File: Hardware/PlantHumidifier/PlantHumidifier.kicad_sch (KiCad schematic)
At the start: 9 parts

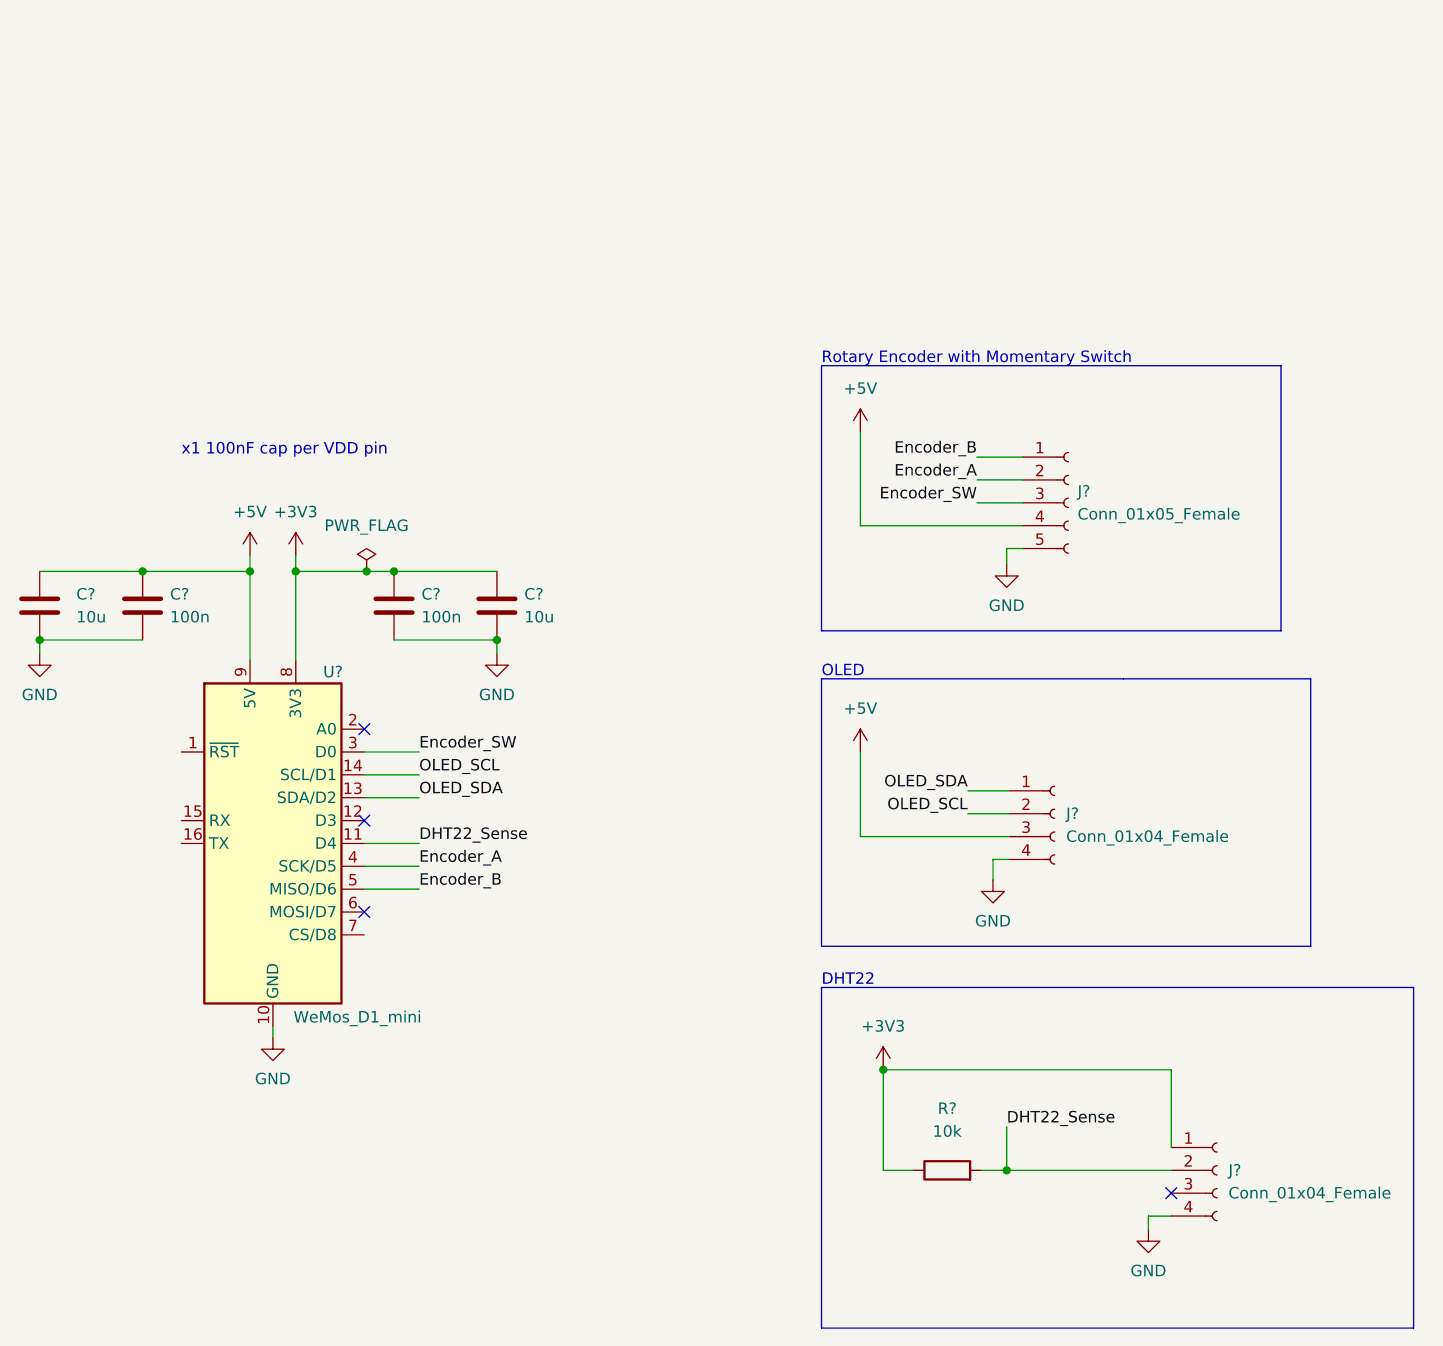
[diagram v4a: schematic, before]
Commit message: Schematic: Finish wiring Grove water atomizer
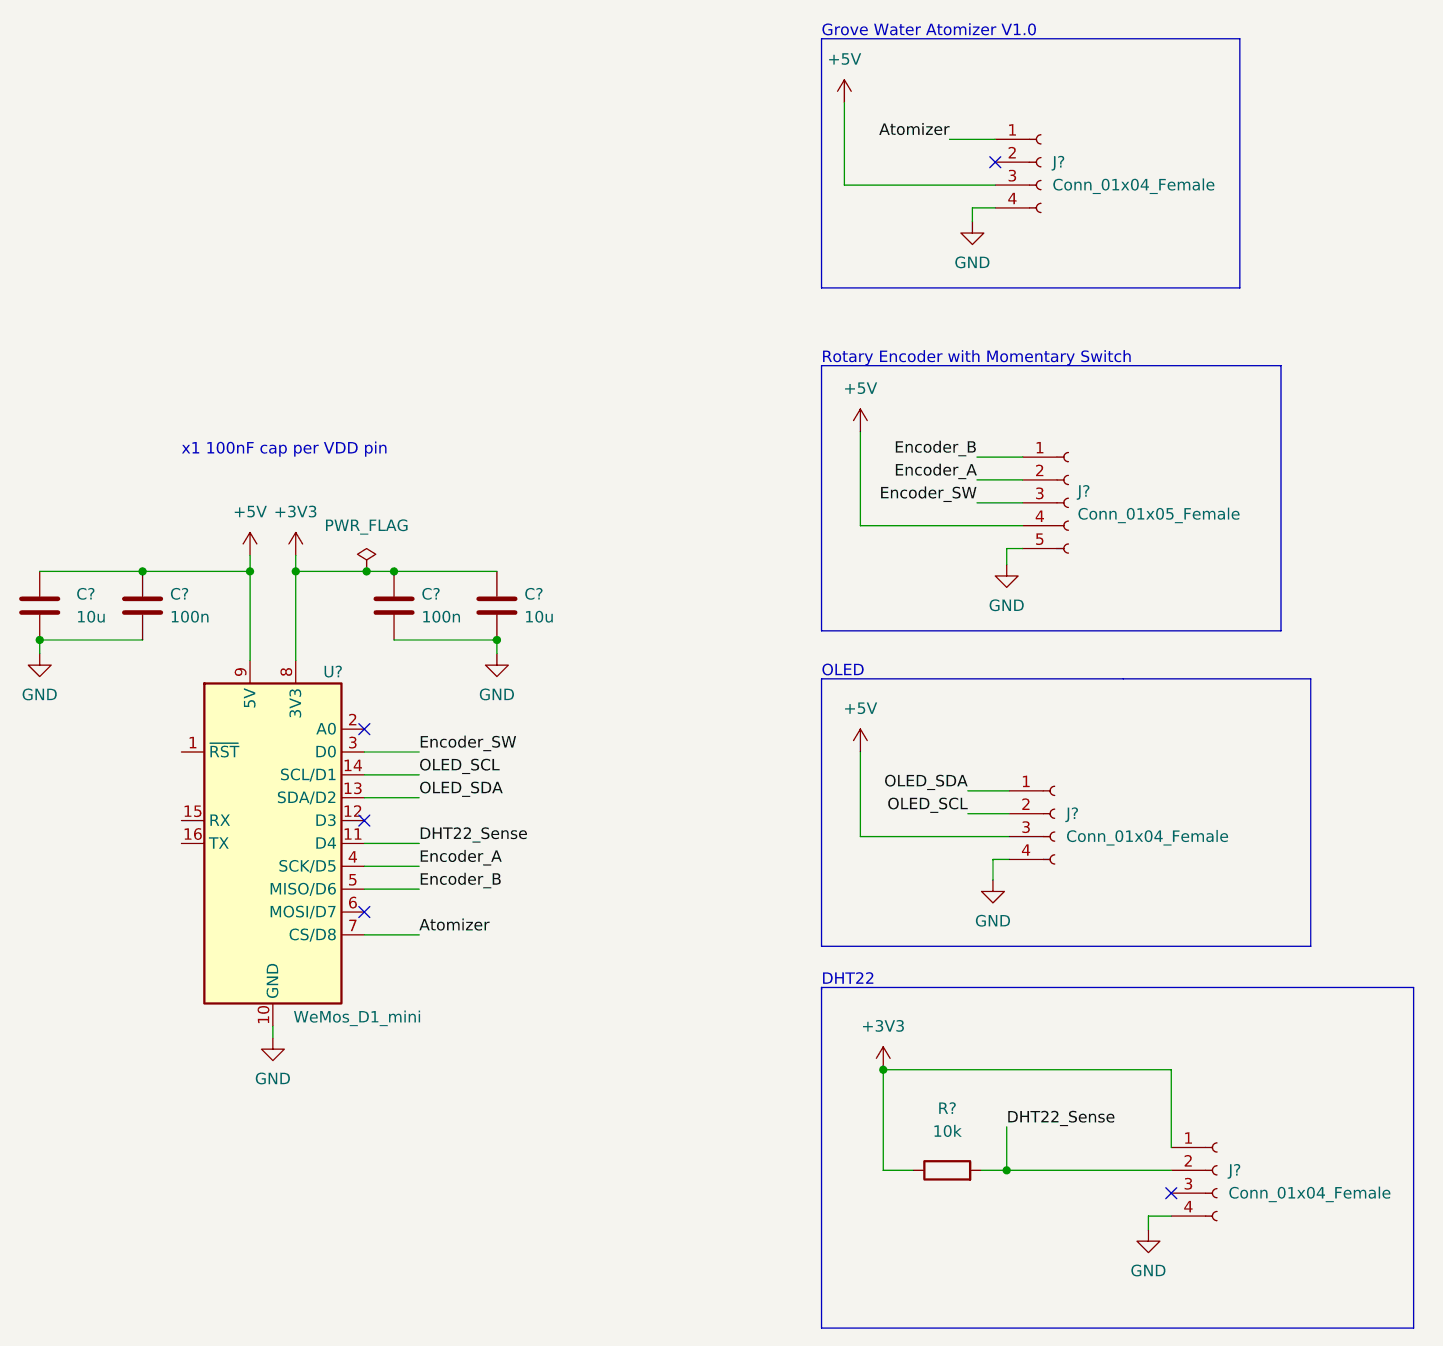
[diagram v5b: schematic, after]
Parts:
- added J?: Conn_01x04_Female, symbol Connector:Conn_01x04_Female
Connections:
- net +5V: now also J?.3 (Pin_3)
- net GND: now also J?.4 (Pin_4)
- net Atomizer: now reaches U?.7 (CS/D8)
- net Atomizer: now also J?.1 (Pin_1)
- no-connect marks 4 -> 5
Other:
- note added: "Grove Water Atomizer V1.0"
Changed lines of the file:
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@@
   (junction (at 164.592 77.724) (diameter 0) (color 0 0 0 0)
   )
+  (no_connect (at 231.394 32.258))
   (no_connect (at 161.29 105.41))
   (no_connect (at 250.952 146.812))
@@
     (stroke (width 0) (type default) (color 0 0 0 0))
   )
+  (wire (pts (xy 228.854 38.862) (xy 228.854 37.338))
+    (stroke (width 0) (type default) (color 0 0 0 0))
+  )
   (polyline (pts (xy 212.09 123.952) (xy 277.876 123.952))
     (stroke (width 0) (type default) (color 0 0 0 0))
@@
     (stroke (width 0) (type default) (color 0 0 0 0))
   )
+  (polyline (pts (xy 258.572 18.542) (xy 212.09 18.542))
+    (stroke (width 0) (type default) (color 0 0 0 0))
+  )
   (wire (pts (xy 228.346 102.108) (xy 232.918 102.108))
     (stroke (width 0) (type default) (color 0 0 0 0))
@@
     (stroke (width 0) (type default) (color 0 0 0 0))
   )
+  (polyline (pts (xy 212.09 18.542) (xy 212.09 46.228))
+    (stroke (width 0) (type default) (color 0 0 0 0))
+  )
   (wire (pts (xy 161.544 77.724) (xy 164.592 77.724))
     (stroke (width 0) (type default) (color 0 0 0 0))
@@
     (stroke (width 0) (type default) (color 0 0 0 0))
   )
+  (wire (pts (xy 226.314 29.718) (xy 231.394 29.718))
+    (stroke (width 0) (type default) (color 0 0 0 0))
+  )
   (wire (pts (xy 161.29 107.95) (xy 167.386 107.95))
     (stroke (width 0) (type default) (color 0 0 0 0))
@@
     (stroke (width 0) (type default) (color 0 0 0 0))
   )
+  (polyline (pts (xy 258.572 46.228) (xy 258.572 18.542))
+    (stroke (width 0) (type default) (color 0 0 0 0))
+  )
   (wire (pts (xy 148.59 77.724) (xy 148.59 87.63))
     (stroke (width 0) (type default) (color 0 0 0 0))
@@
     (stroke (width 0) (type default) (color 0 0 0 0))
   )
+  (wire (pts (xy 161.29 118.11) (xy 167.386 118.11))
+    (stroke (width 0) (type default) (color 0 0 0 0))
+  )
+  (polyline (pts (xy 212.09 46.228) (xy 258.572 46.228))
+    (stroke (width 0) (type default) (color 0 0 0 0))
+  )
   (wire (pts (xy 125.222 77.724) (xy 136.652 77.724))
     (stroke (width 0) (type default) (color 0 0 0 0))
@@
     (stroke (width 0) (type default) (color 0 0 0 0))
   )
+  (wire (pts (xy 214.63 25.654) (xy 214.63 34.798))
+    (stroke (width 0) (type default) (color 0 0 0 0))
+  )
   (wire (pts (xy 161.29 102.87) (xy 167.386 102.87))
     (stroke (width 0) (type default) (color 0 0 0 0))
   )
+  (wire (pts (xy 228.854 37.338) (xy 231.394 37.338))
+    (stroke (width 0) (type default) (color 0 0 0 0))
+  )
   (wire (pts (xy 218.948 144.272) (xy 222.25 144.272))
     (stroke (width 0) (type default) (color 0 0 0 0))
@@
     (stroke (width 0) (type default) (color 0 0 0 0))
   )
+  (wire (pts (xy 214.63 34.798) (xy 231.394 34.798))
+    (stroke (width 0) (type default) (color 0 0 0 0))
+  )
   (wire (pts (xy 161.29 100.33) (xy 167.386 100.33))
     (stroke (width 0) (type default) (color 0 0 0 0))
@@
   )
   (text "DHT22" (at 212.09 123.952 0)
+    (effects (font (size 1.27 1.27)) (justify left bottom))
+  )
+  (text "Grove Water Atomizer V1.0" (at 212.09 18.542 0)
     (effects (font (size 1.27 1.27)) (justify left bottom))
   )
@@
   )
   (label "DHT22_Sense" (at 232.664 139.446 0)
+    (effects (font (size 1.27 1.27)) (justify left bottom))
+  )
+  (label "Atomizer" (at 226.314 29.718 180)
+    (effects (font (size 1.27 1.27)) (justify right bottom))
+  )
+  (label "Atomizer" (at 167.386 118.11 0)
     (effects (font (size 1.27 1.27)) (justify left bottom))
   )
@@
     (pin "2")
   )
+  (symbol (lib_id "Connector:Conn_01x04_Female") (at 236.474 32.258 0) (unit 1)
+    (in_bom yes) (on_board yes) (fields_autoplaced)
+    (property "Reference" "J?" (id 0) (at 237.744 32.2579 0)
+      (effects (font (size 1.27 1.27)) (justify left))
+    )
+    (property "Value" "Conn_01x04_Female" (id 1) (at 237.744 34.7979 0)
+      (effects (font (size 1.27 1.27)) (justify left))
+    )
+    (property "Footprint" "" (id 2) (at 236.474 32.258 0)
+      (effects (font (size 1.27 1.27)) hide)
+    )
+    (property "Datasheet" "~" (id 3) (at 236.474 32.258 0)
+      (effects (font (size 1.27 1.27)) hide)
+    )
+    (pin "1")
+    (pin "2")
+    (pin "3")
+    (pin "4")
+  )
+  (symbol (lib_id "power:+5V") (at 214.63 25.654 0) (unit 1)
+    (in_bom yes) (on_board yes) (fields_autoplaced)
+    (property "Reference" "#PWR?" (id 0) (at 214.63 29.464 0)
+      (effects (font (size 1.27 1.27)) hide)
+    )
+    (property "Value" "+5V" (id 1) (at 214.63 20.828 0))
+    (property "Footprint" "" (id 2) (at 214.63 25.654 0)
+      (effects (font (size 1.27 1.27)) hide)
+    )
+    (property "Datasheet" "" (id 3) (at 214.63 25.654 0)
+      (effects (font (size 1.27 1.27)) hide)
+    )
+    (pin "1")
+  )
   (symbol (lib_id "power:GND") (at 232.664 76.962 0) (unit 1)
     (in_bom yes) (on_board yes) (fields_autoplaced)
@@
     (pin "3")
     (pin "4")
+  )
+  (symbol (lib_id "power:GND") (at 228.854 38.862 0) (unit 1)
+    (in_bom yes) (on_board yes) (fields_autoplaced)
+    (property "Reference" "#PWR?" (id 0) (at 228.854 45.212 0)
+      (effects (font (size 1.27 1.27)) hide)
+    )
+    (property "Value" "GND" (id 1) (at 228.854 43.434 0))
+    (property "Footprint" "" (id 2) (at 228.854 38.862 0)
+      (effects (font (size 1.27 1.27)) hide)
+    )
+    (property "Datasheet" "" (id 3) (at 228.854 38.862 0)
+      (effects (font (size 1.27 1.27)) hide)
+    )
+    (pin "1")
   )
   (symbol (lib_id "Device:R") (at 226.06 144.272 90) (unit 1)
@@
       (reference "#PWR?") (unit 1) (value "GND") (footprint "")
     )
+    (path "/4785a3cc-0fe4-4430-87e9-db5027174a62"
+      (reference "#PWR?") (unit 1) (value "+5V") (footprint "")
+    )
     (path "/4f59d960-e3e5-4142-af04-748d258b5a1b"
       (reference "#PWR?") (unit 1) (value "GND") (footprint "")
@@
       (reference "#PWR?") (unit 1) (value "+5V") (footprint "")
     )
+    (path "/9e6365a1-ed0a-4dd0-9ad9-70f3870d754a"
+      (reference "#PWR?") (unit 1) (value "GND") (footprint "")
+    )
     (path "/e3933081-4e4f-42b2-bbd3-5138b562a407"
       (reference "#PWR?") (unit 1) (value "+3V3") (footprint "")
@@
       (reference "C?") (unit 1) (value "10u") (footprint "")
     )
+    (path "/2394e559-b98a-40f6-b850-791be34e4734"
+      (reference "J?") (unit 1) (value "Conn_01x04_Female") (footprint "")
+    )
     (path "/83845b8d-1c62-4450-bceb-8208d6b21664"
